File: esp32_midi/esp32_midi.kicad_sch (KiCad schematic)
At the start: 22 parts, among them J2 5V-12V, SW1 SW_SPST, U1 ESP32-S3-WROOM-2, U3 AMS1117-3.3

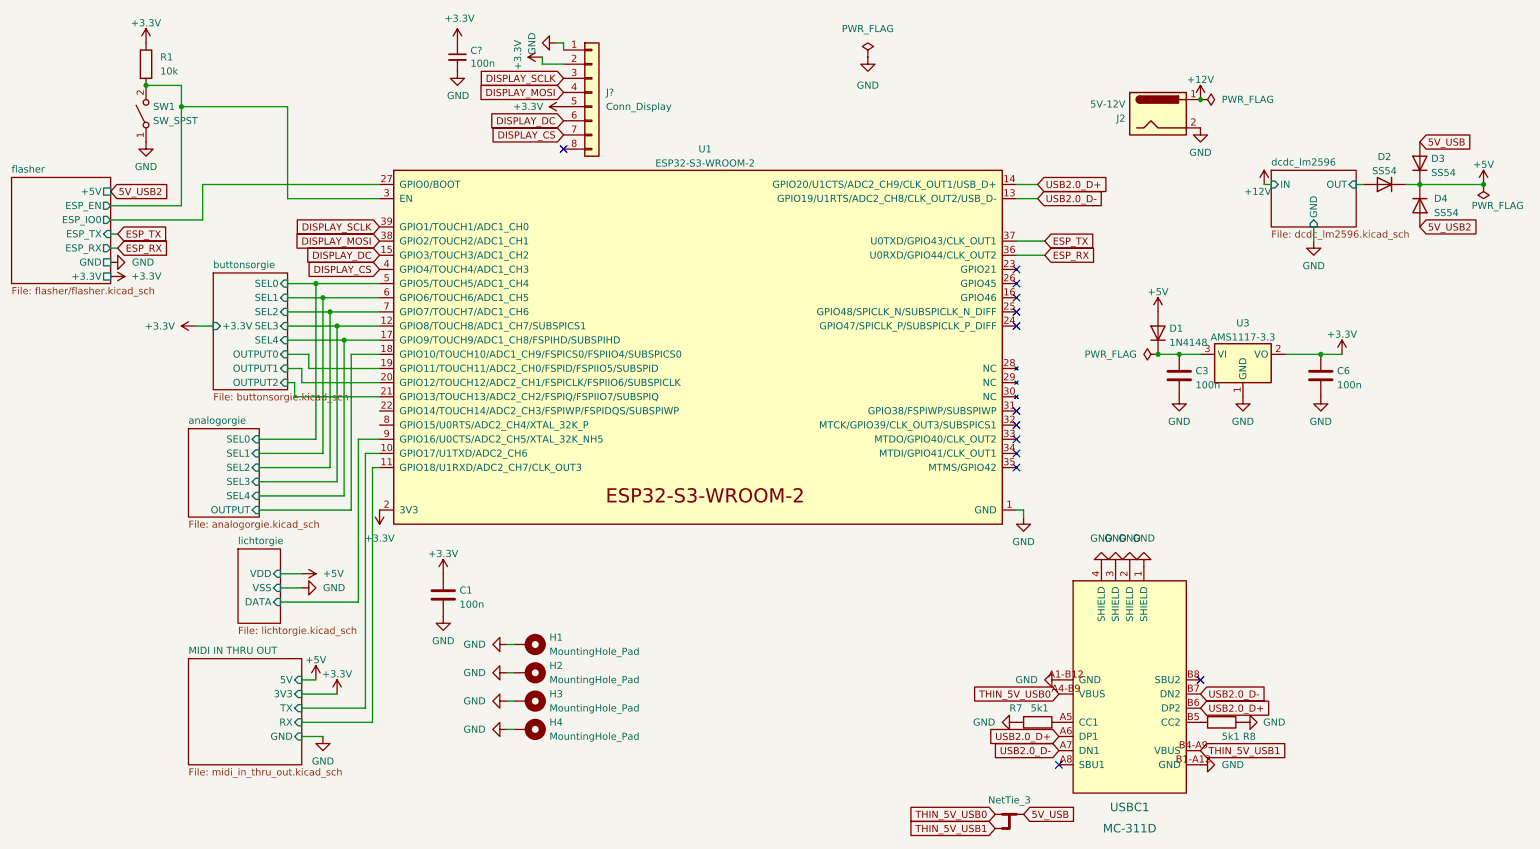
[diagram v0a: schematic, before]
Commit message: Update parts numbers
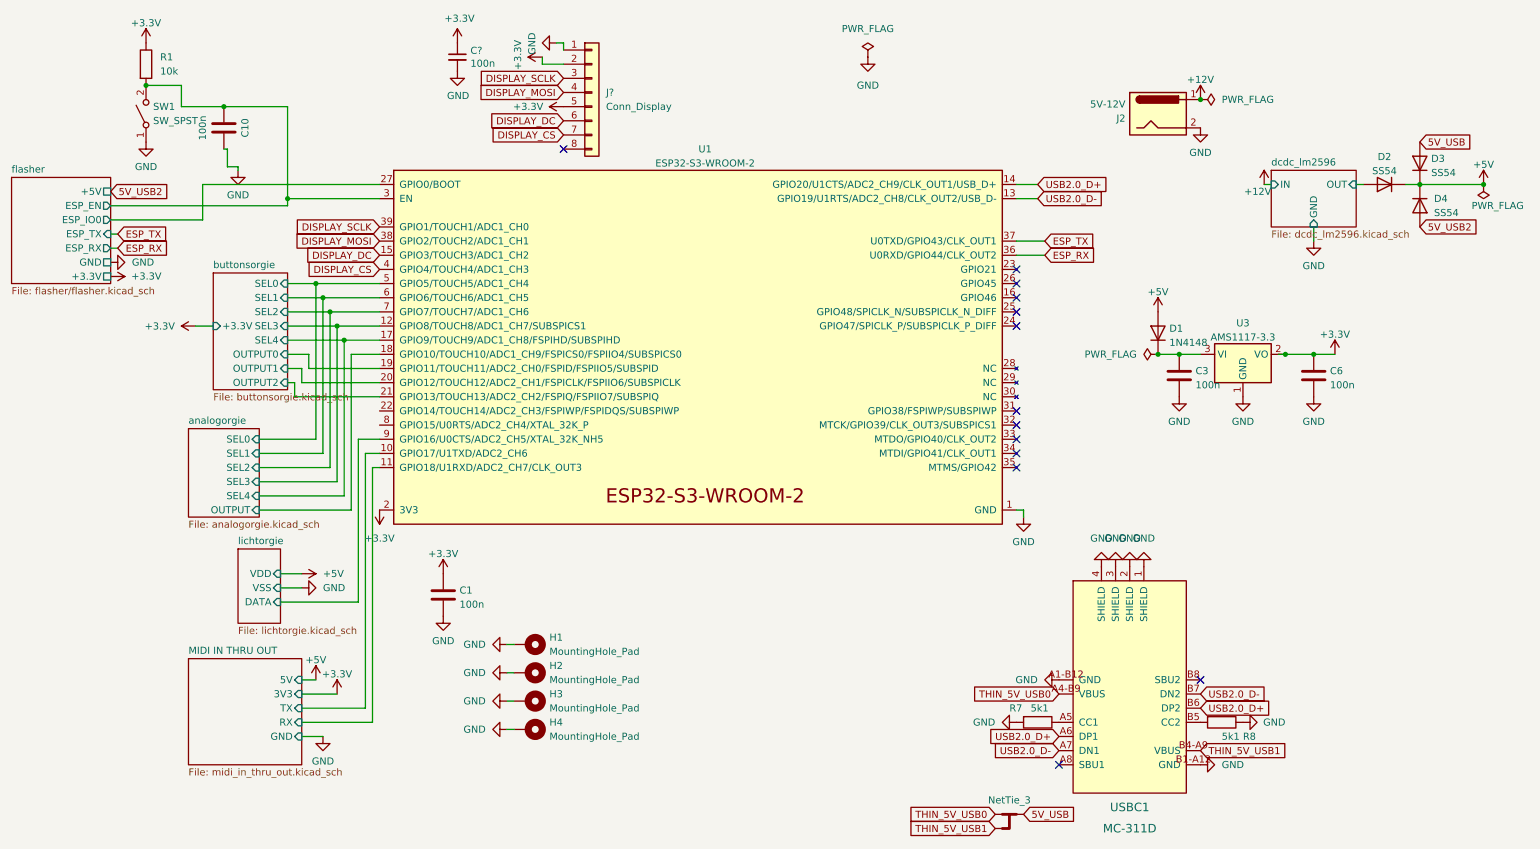
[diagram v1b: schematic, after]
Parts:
- added C10: 100n, Capacitor_SMD:C_1206_3216Metric, symbol Device:C
- C1: Field-1 (none) -> C24497; LCSC (none) -> C1
- C3: Field-1 (none) -> C24497; LCSC (none) -> C3
- C6: Field-1 (none) -> C24497; LCSC (none) -> C6
- C?: Field-1 (none) -> ${DNP}; LCSC Part # C1525 -> C24497
- D1: Field-1 (none) -> ${DNP}; LCSC (none) -> C81598
- D2, D3, D4: Field-1 (none) -> ${DNP}; LCSC (none) -> C22452
- H1, H2, H3, H4, J2, J?, NT102, SW1, U1: Field-1 (none) -> ${DNP}
- R1: Field-1 (none) -> ${DNP}; LCSC (none) -> C17902
- R7, R8: Field-1 (none) -> ${DNP}; LCSC (none) -> C25905
- U3: Field-1 (none) -> ${DNP}; LCSC (none) -> C6186
- USBC1: Field-1 (none) -> ${DNP}; LCSC (none) -> C136423
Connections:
- net GND: now also C10.1
- net flasher/ESP_EN: now also C10.2
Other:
- moved on the sheet: C6
